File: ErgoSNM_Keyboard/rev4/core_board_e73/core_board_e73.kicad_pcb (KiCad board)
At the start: 2 copper layers, 50.8 x 36.2 mm, 55 parts, among them J1 USB_C_Receptacle_USB2.0, J2 USB_C_Receptacle_USB2.0, J3 Conn_01x30, J4 Conn_Batt, J5 Debug, SW1 SW_DPDT_x2, U1 E73-2G4M08S1C, U2 SRV05-4, U3 TPS63020, U4 BQ24075RGT, U5 SRV05-4, Y1 32.768kHz

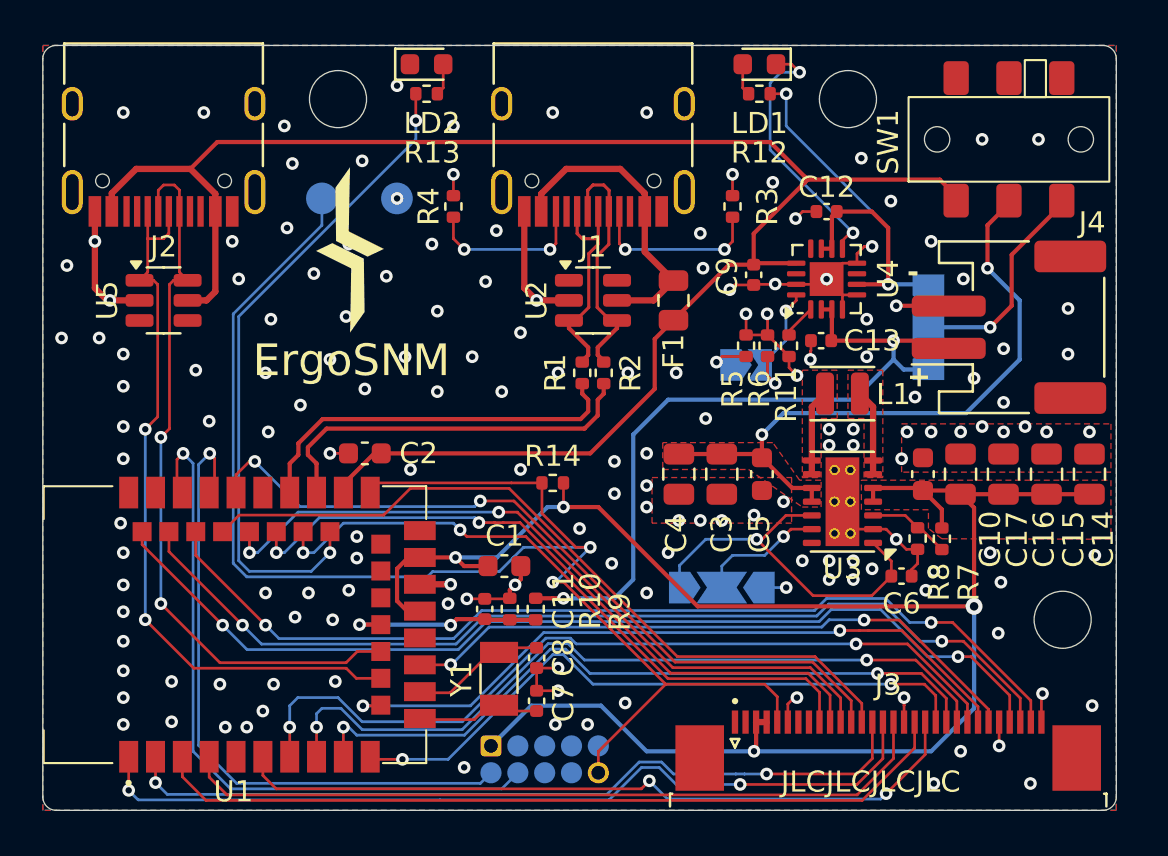
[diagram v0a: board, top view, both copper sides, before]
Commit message: feat: update USB ESD
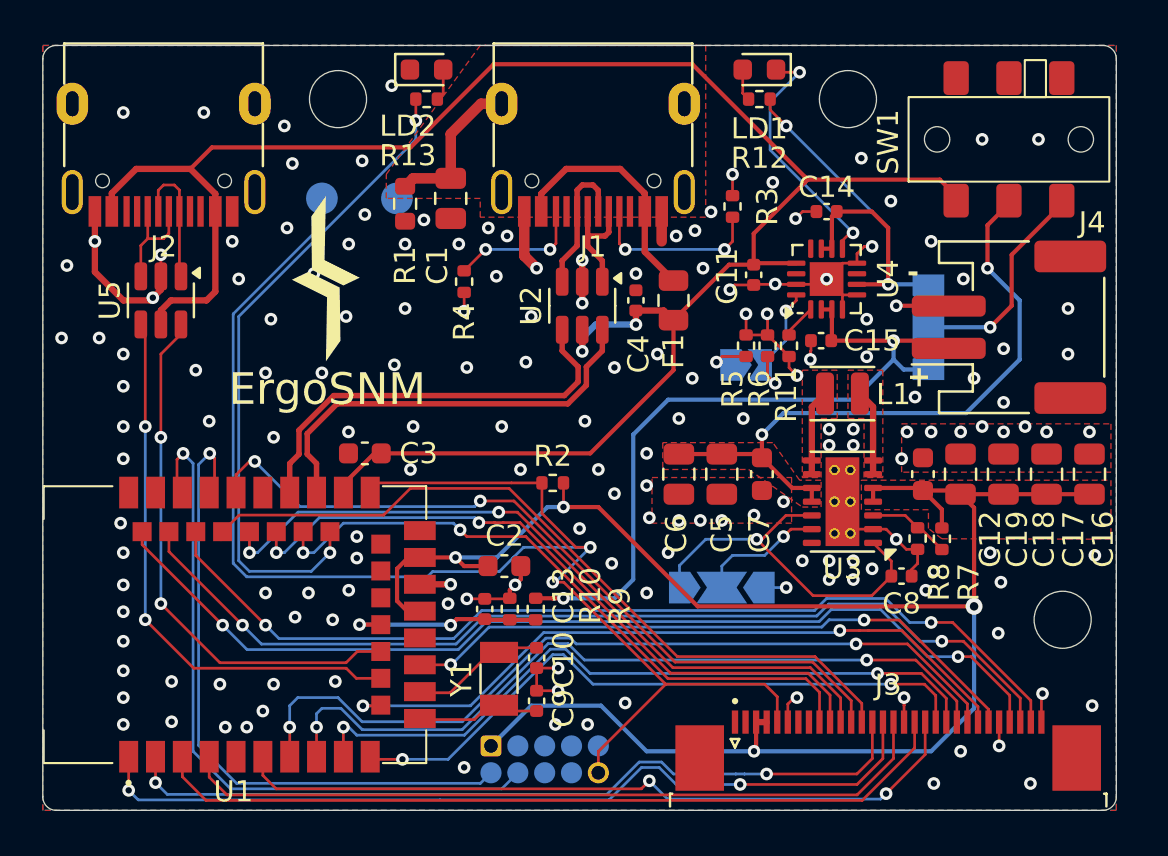
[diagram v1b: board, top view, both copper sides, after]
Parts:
- removed the R2 at (142.7, 100.6)
- added C1: 4.7nF, Capacitor_SMD:C_0805_2012Metric, F.Cu at (135.5, 92.3)
- added C4: 100nF, Capacitor_SMD:C_0402_1005Metric, F.Cu at (144.3, 97.2)
- R1: value 27R -> 1M; footprint Resistor_SMD:R_0402_1005Metric -> Resistor_SMD:R_0603_1608Metric
- R3, R4: value 5.1k -> 5.1k 1%
- U2, U5: value SRV05-4 -> USBLC6-2SC6
- moved R1 11.6 mm to (133.3, 92.6), turned to -90 degrees
- moved R4 3.59 mm to (136.1, 96.3), turned to -90 degrees
- moved U2 0.57 mm to (141.7, 97.4), turned to -90 degrees
- moved LD1 0.25 mm to (150.1, 86.2)
- moved LD2 0.25 mm to (134.4, 86.2)
- moved R12 0.25 mm to (150.1, 87.6)
- moved R13 0.25 mm to (134.4, 87.6)
- moved U5 0.13 mm to (121.8, 97.2), turned to -90 degrees
- renumbered C8 to C10, C9 to C11, C10 to C12, C11 to C13, C12 to C14, C13 to C15, C14 to C16, C15 to C17, C16 to C18, C17 to C19, C1 to C2, C2 to C3, C3 to C5, C4 to C6, C5 to C7, C6 to C8, C7 to C9, R14 to R2
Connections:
- J1 pad A6: USB_D+ -> /CONN_D+
- J1 pad A7: USB_D- -> /CONN_D-
- J1 pad B6: USB_D+ -> /CONN_D+
- J1 pad B7: USB_D- -> /CONN_D-
- J1 pad S1: GND -> /USB_SH
- J2 pad A6: TX -> Net-(J2-D+-PadA6)
- J2 pad A7: RX -> Net-(J2-D--PadA7)
- J2 pad B6: TX -> Net-(J2-D+-PadA6)
- J2 pad B7: RX -> Net-(J2-D--PadA7)
- R1 pad 1: /D+ -> /USB_SH
- R1 pad 2: USB_D+ -> GND
- U1 pad 29: /D- -> USB_D-
- U1 pad 31: /D+ -> USB_D+
- U2 pad 1: unconnected-(U2-IO1-Pad1) -> /CONN_D-
- U2 pad 3: USB_D+ -> /CONN_D+
- U2 pad 4: USB_D- -> USB_D+
- U2 pad 5: +5V -> VBUS
- U2 pad 6: unconnected-(U2-IO4-Pad6) -> USB_D-
- U5 pad 1: TX -> Net-(J2-D--PadA7)
- U5 pad 3: unconnected-(U5-IO2-Pad3) -> Net-(J2-D+-PadA6)
- U5 pad 4: unconnected-(U5-IO3-Pad4) -> TX
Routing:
- net /D-: track 18.8 -> 0.00 mm
- net /D+: track 18.8 -> 0.00 mm
- net VBUS: track 83.8 -> 96.0 mm, vias 0 -> 2
- net USB_D+: track 10.5 -> 20.6 mm
- net RX: track 34.6 -> 25.4 mm
- net USB_D-: track 11.7 -> 20.6 mm
- net TX: track 34.9 -> 26.4 mm
- net /USB_SH: track 0.00 -> 7.38 mm
- net /CONN_D+: track 0.00 -> 6.83 mm
- net Net-(J2-D--PadA7): track 0.00 -> 6.32 mm
- net /CONN_D-: track 0.00 -> 5.67 mm
- net Net-(J2-D+-PadA6): track 0.00 -> 5.35 mm
- net +5V: track 14.5 -> 11.4 mm
- net GND: track 54.1 -> 56.0 mm, vias 162 -> 168
- net Net-(J1-CC2): track 7.71 -> 6.40 mm
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- added copper zone on F.Cu, net /USB_SH
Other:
- board text added: "Unit: mm"

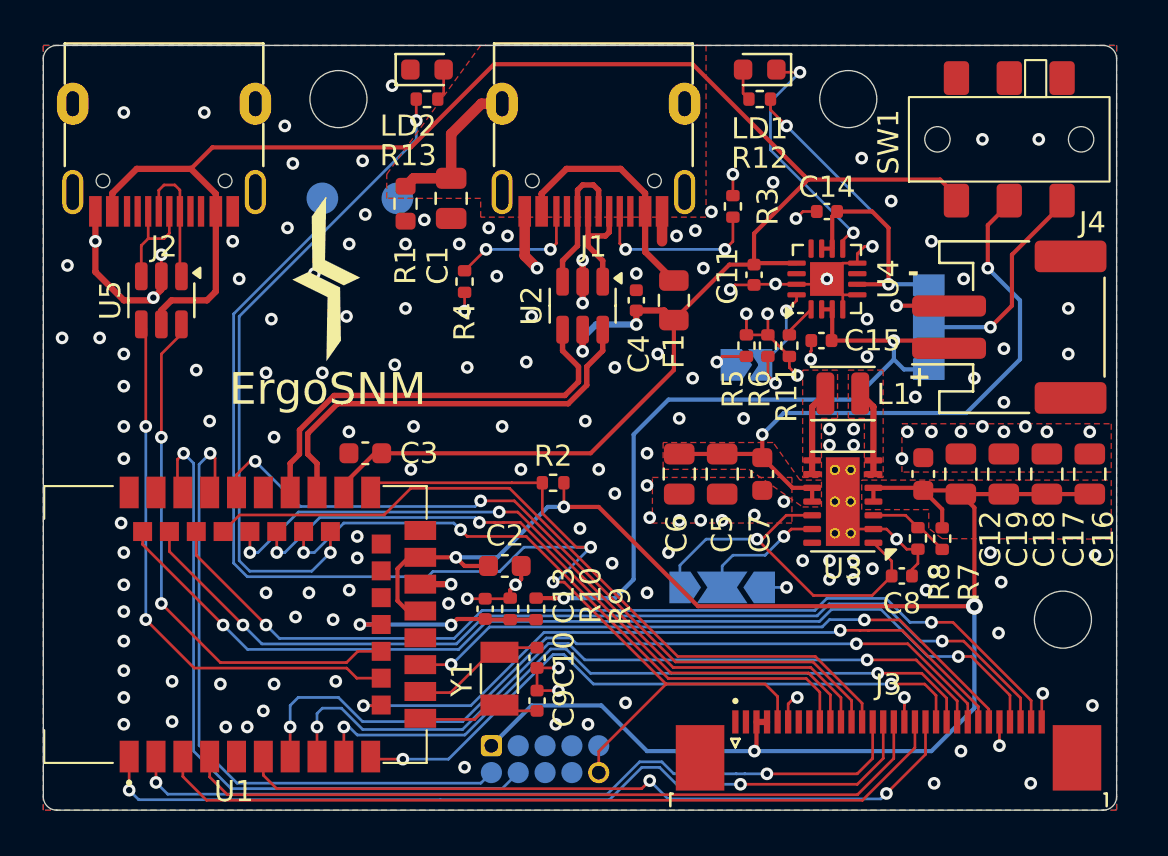
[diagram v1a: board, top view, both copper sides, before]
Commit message: feat: change Buck-Boost DC/DC IC from TPS63020 to TPS63900
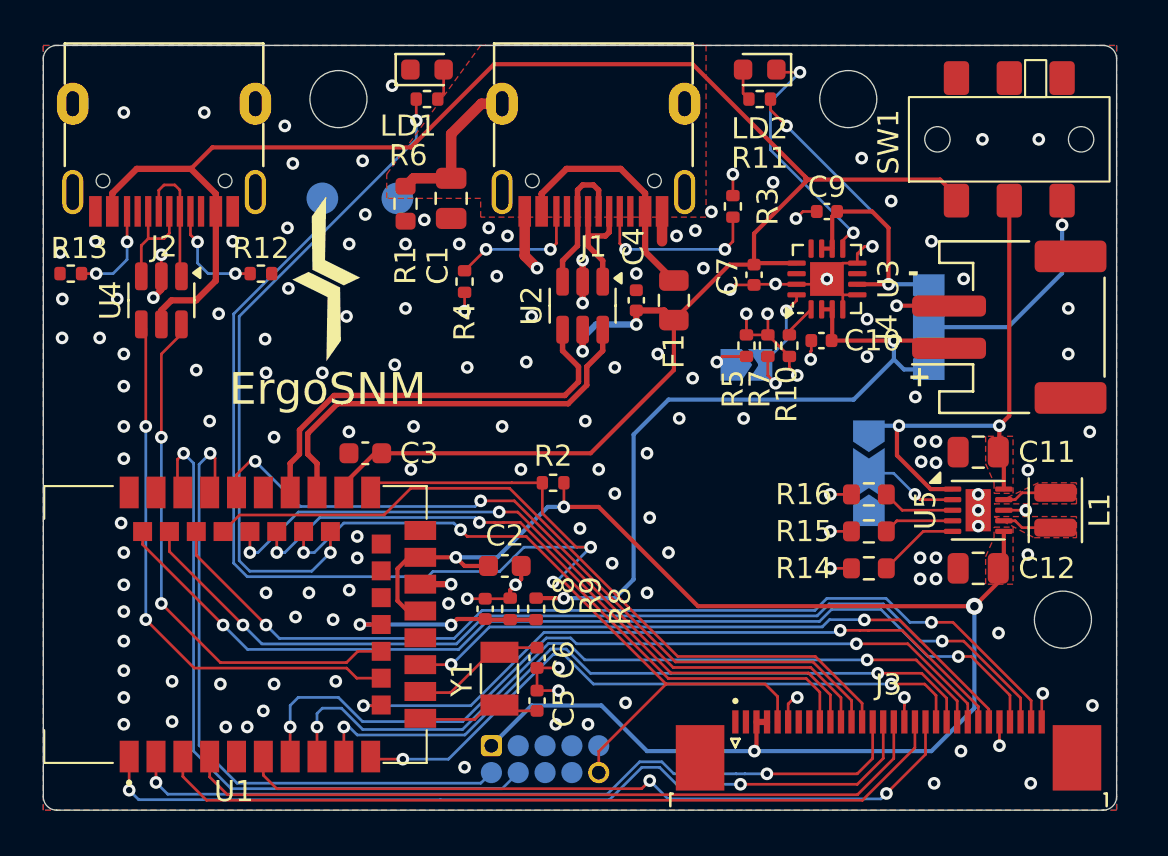
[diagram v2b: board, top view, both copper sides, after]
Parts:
- removed C16, C17, C18, C19: 22uF, Capacitor_SMD:C_0805_2012Metric
- removed the C5 at (148.3, 105.4)
- removed the C6 at (146.3, 105.4)
- removed the C7 at (150.2, 105.4)
- removed the C8 at (156.8, 110.2)
- removed the R7 at (158.8, 108.4)
- removed the R8 at (157.6, 108.4)
- removed the U3 at (154.0, 106.7)
- added C11: 22uF, Capacitor_SMD:C_0805_2012Metric, F.Cu at (160.5, 104.3)
- added R12: 5.1k 1%, Resistor_SMD:R_0402_1005Metric, F.Cu at (126.5, 95.9)
- added R13: 5.1k 1%, Resistor_SMD:R_0402_1005Metric, F.Cu at (117.5, 95.9)
- added R14: 1.2k 1%, Resistor_SMD:R_0603_1608Metric, F.Cu at (155.3, 109.8)
- added R15: 0R 1%, Resistor_SMD:R_0603_1608Metric, F.Cu at (155.3, 108.1)
- added R16: 30k 1%, Resistor_SMD:R_0603_1608Metric, F.Cu at (155.3, 106.3)
- added U5: TPS63900, Package_SON:WSON-10-1EP_2.5x2.5mm_P0.5mm_EP1.2x2mm, F.Cu at (160.5, 107.1)
- C12: value 2.2uF -> 22uF; footprint Capacitor_SMD:C_0603_1608Metric -> Capacitor_SMD:C_0805_2012Metric
- L1: value 1.5uH -> 2.2uH
- SB3: renamed from SB2; value Power Save -> VDD Selection
- moved L1 11.5 mm to (164.1, 107.1), turned to 90 degrees
- moved SB3 8.80 mm to (155.3, 105.3), turned to -90 degrees
- moved C12 5.17 mm to (160.5, 109.8), turned to 180 degrees
- turned C4 to 90 degrees
- renumbered C15 to C10, C9 to C5, C10 to C6, C11 to C7, C13 to C8, C14 to C9, LD2 to LD1, LD1 to LD2, R11 to R10, R12 to R11, R13 to R6, R6 to R7, R9 to R8, R10 to R9, SB3 to SB1, SB1 to SB2, U4 to U3, U5 to U4
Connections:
- C4 pad 1: GND -> VBUS
- C4 pad 2: VBUS -> GND
- J2 pad A5: unconnected-(J2-CC1-PadA5) -> Net-(J2-CC1)
- J2 pad B5: unconnected-(J2-CC2-PadB5) -> Net-(J2-CC2)
- J3 pad MP: (no net) -> unconnected-(J3-MountPin-PadMP)_1
- J4 pad MP: (no net) -> unconnected-(J4-MountPin-PadMP)
- SB3 pad 1: /VINA -> /VIN_DCDC
- SB3 pad 2: /PWR_SAVE -> /VDD_SEL
- SW1 pad 2: Net-(SW1A-B) -> /VIN_DCDC
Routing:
- net Net-(SW1A-B): track 30.9 -> 0.00 mm, vias 2 -> 0
- net /VIN_DCDC: track 0.00 -> 25.0 mm, vias 0 -> 2
- net /VINA: track 18.1 -> 0.00 mm, vias 1 -> 0
- net VDD: track 87.6 -> 73.0 mm
- net GND: track 56.0 -> 47.7 mm, vias 168 -> 153
- net /PWR_SAVE: track 6.00 -> 0.00 mm, vias 1 -> 0
- net Net-(J2-CC1): track 0.00 -> 5.28 mm, vias 0 -> 2
- net Net-(J2-CC2): track 0.00 -> 4.71 mm, vias 0 -> 2
- net /VDD_SEL: track 0.00 -> 4.48 mm, vias 0 -> 1
- net Net-(U3-FB): track 3.92 -> 0.00 mm
- net Net-(U5-CFG3): track 0.00 -> 3.86 mm
- net Net-(U5-CFG1): track 0.00 -> 3.45 mm
- net Net-(U5-CFG2): track 0.00 -> 3.34 mm
- net Net-(U5-LX2): track 4.07 -> 2.57 mm
- net Net-(U5-LX1): track 4.07 -> 2.57 mm
- added copper zone on F.Cu, net /VIN_DCDC
- removed copper zone on F.Cu, net Net-(SW1A-B)

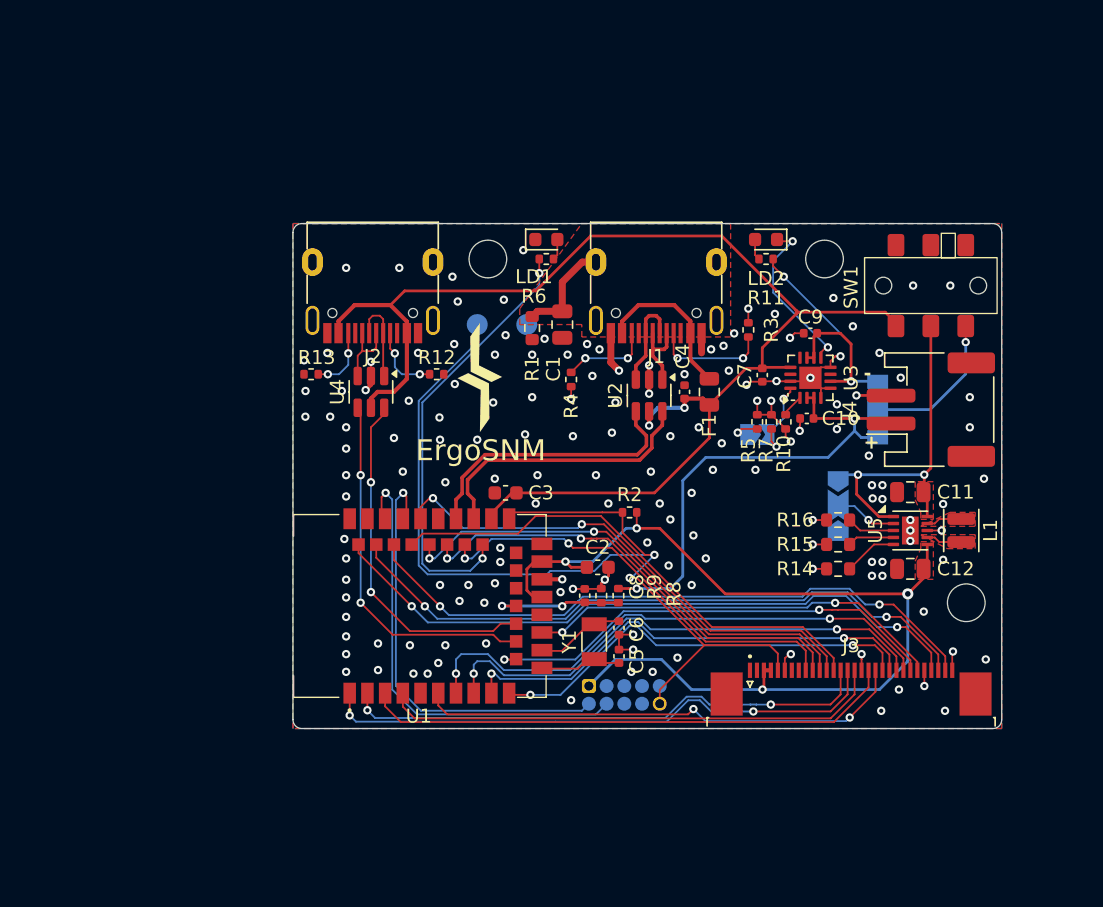
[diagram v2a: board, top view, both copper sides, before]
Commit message: feat: change pin header position
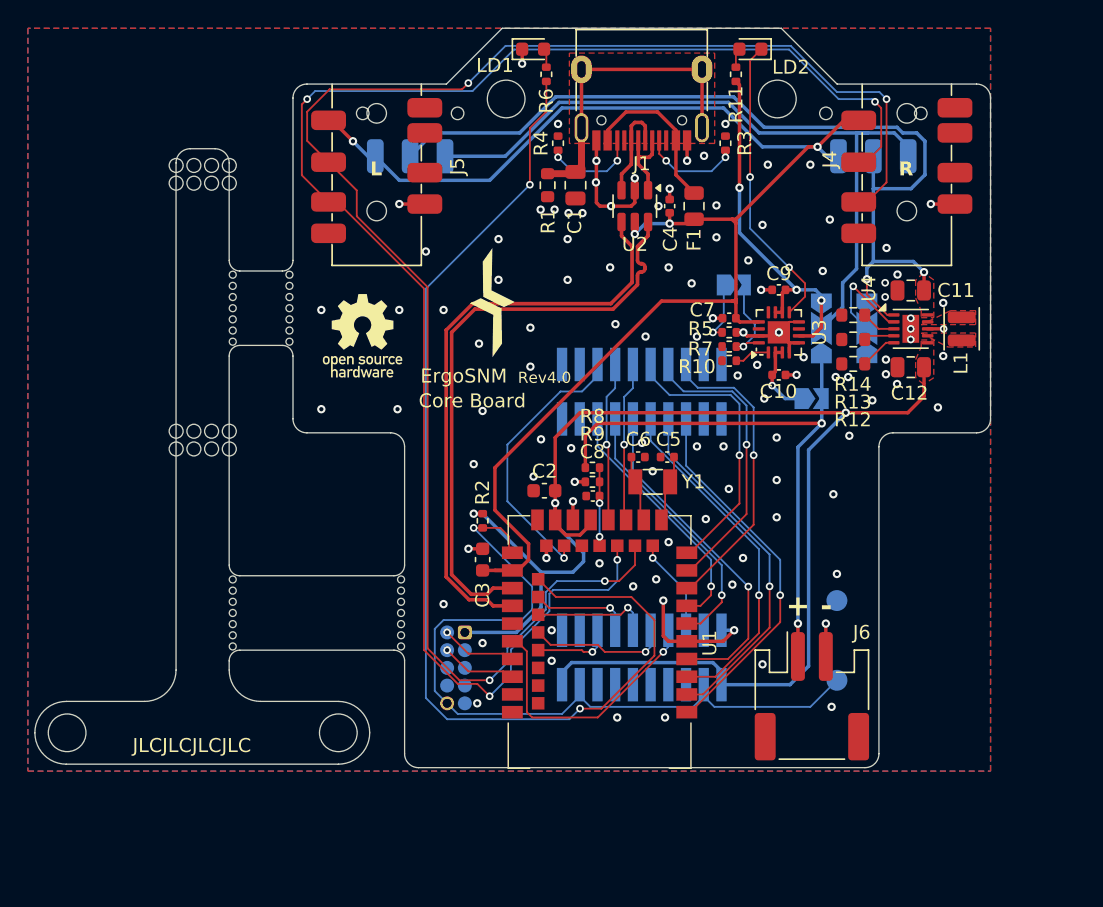
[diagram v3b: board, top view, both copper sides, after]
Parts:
- removed the R12 at (126.5, 95.9)
- removed the R13 at (117.5, 95.9)
- removed the U4 at (121.8, 97.2)
- added H23: MountingHole, ErgoSNM_Keyboard:mouse_bit, F.Cu at (111.9, 113.0)
- added H4: MountingHole, MountingHole:MountingHole_2.7mm_M2.5_ISO7380, F.Cu at (100.0, 121.6)
- added H5: MountingHole, ErgoSNM_Keyboard:mouse_bit, F.Cu at (111.9, 91.2)
- added H6: MountingHole, ErgoSNM_Keyboard:mouse_bit, F.Cu at (116.0, 91.2)
- added H7: MountingHole, ErgoSNM_Keyboard:mouse_bit, F.Cu at (124.0, 113.0)
- added J4: PJ-393_TRRS_8P, ErgoSNM_Keyboard:PJ-393 8P TRRS, F.Cu at (160.2, 80.5)
- added J5: PJ-393_TRRS_8P, ErgoSNM_Keyboard:PJ-393 8P TRRS, F.Cu at (122.2, 80.5)
- added J8: Conn_02x05_Odd_Even, Connector_PinHeader_1.27mm:PinHeader_2x04_P1.27mm_Vertical, F.Cu at (111.6, 100.0)
- added J9: Conn_02x05_Odd_Even, Connector_PinHeader_1.27mm:PinHeader_2x04_P1.27mm_Vertical, F.Cu at (111.6, 80.9)
- added SB2: LiPo_CHG, Jumper:SolderJumper-2_P1.3mm_Open_TrianglePad1.0x1.5mm, B.Cu at (153.4, 97.6)
- added SW2: SW_SPDT, ErgoSNM_Keyboard:9_3.5_3.5_switch, B.Cu at (124.6, 77.2)
- J2: value USB_C_Receptacle_USB2.0 -> Conn_02x10_Odd_Even; footprint Connector_USB:USB_C_Receptacle_HRO_TYPE-C-31-M-12 -> Connector_PinHeader_1.27mm:PinHeader_2x10_P1.27mm_Vertical_SMD; moved to B.Cu
- J3: value Conn_01x30 -> Conn_02x10_Odd_Even; footprint Connector_FFC-FPC:TE_3-1734839-0_1x30-1MP_P0.5mm_Horizontal -> Connector_PinHeader_1.27mm:PinHeader_2x10_P1.27mm_Vertical_SMD; moved to B.Cu
- SW1: value SW_DPDT_x2 -> SW_SPDT; footprint ErgoSNM_Keyboard:MSKT-22D14-T -> ErgoSNM_Keyboard:9_3.5_3.5_switch; moved to B.Cu
- moved H3 46.0 mm to (119.5, 121.6)
- moved TP1 36.3 mm to (155.2, 117.8)
- moved TP2 29.8 mm to (155.2, 112.1)
- moved H2 25.5 mm to (131.5, 76.2)
- moved H1 23.7 mm to (150.9, 76.2)
- moved J6 22.2 mm to (153.4, 119.0), turned to 0 degrees
- moved J2 21.0 mm to (141.2, 97.1), turned to 90 degrees
- moved R4 17.0 mm to (135.2, 79.3), turned to 90 degrees
- moved J3 15.2 mm to (141.2, 116.2), turned to 90 degrees
- moved R12 14.7 mm to (156.4, 95.1)
- moved R13 14.7 mm to (156.4, 93.4)
- moved R14 14.7 mm to (156.4, 91.6)
- moved C5 14.7 mm to (143.0, 101.8), turned to 0 degrees
- moved C11 14.5 mm to (160.5, 89.9)
- moved C12 14.5 mm to (160.5, 95.4)
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- renumbered J4 to J6, J5 to J7, R14 to R12, R15 to R13, R16 to R14, SB2 to SB3, SB3 to SB4, U5 to U4
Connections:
- net /VDD_SEL renamed /OUT_SEL
- net Net-(SB2-C) renamed /VBATT_SRC
- C10 pad 2: +BATT -> Net-(SB2-A)
- J3 pad 1: unconnected-(J3-Pin_1-Pad1) -> VDD
- J3 pad 10: SCLK -> HS_IO_2
- J3 pad 11: MOSI -> unconnected-(J3-Pin_11-Pad11)
- J3 pad 12: MISO -> HS_IO_3
- J3 pad 13: nCS -> unconnected-(J3-Pin_13-Pad13)
- J3 pad 14: ROW_0 -> HS_IO_4
- J3 pad 15: ROW_1 -> unconnected-(J3-Pin_15-Pad15)
- J3 pad 16: ROW_2 -> HS_IO_5
- J3 pad 17: GND -> RESET
- J3 pad 18: ROW_3 -> unconnected-(J3-Pin_18-Pad18)
- J3 pad 19: ROW_4 -> VDD
- J3 pad 2: unconnected-(J3-Pin_2-Pad2) -> GND
- J3 pad 20: COL_0 -> GND
- J3 pad 3: VDD -> RESET
- J3 pad 4: VDD -> unconnected-(J3-Pin_4-Pad4)
- J3 pad 5: RESET -> unconnected-(J3-Pin_5-Pad5)
- J3 pad 6: GND -> HS_IO_0
- J3 pad 8: unconnected-(J3-Pin_8-Pad8) -> HS_IO_1
- J3 pad 9: MOTION -> unconnected-(J3-Pin_9-Pad9)
- SB4 pad 1: /VIN_DCDC -> GND
- SB4 pad 3: GND -> /VIN_DCDC
- U1 pad 1: ROW_1 -> ROW_IO_0
- U1 pad 10: COL_0 -> COL_IO_2
- U1 pad 12: COL_4 -> HS_IO_0
- U1 pad 15: COL_5 -> COL_IO_3
- U1 pad 17: unconnected-(U1-P1.09-Pad17) -> COL_IO_4
- U1 pad 2: ROW_0 -> ROW_IO_1
- U1 pad 22: unconnected-(U1-P0.07-Pad22) -> COL_IO_5
- U1 pad 3: ROW_3 -> ROW_IO_2
- U1 pad 30: MOTION -> HS_IO_4
- U1 pad 32: SCLK -> HS_IO_3
- U1 pad 34: MOSI -> HS_IO_2
- U1 pad 35: MISO -> HS_IO_1
- U1 pad 36: nCS -> HS_IO_5
- U1 pad 38: IO_2 -> unconnected-(U1-P1.02-Pad38)
- U1 pad 4: ROW_2 -> ROW_IO_3
- U1 pad 40: IO_1 -> unconnected-(U1-P1.04-Pad40)
- U1 pad 42: IO_0 -> unconnected-(U1-P1.06-Pad42)
- U1 pad 6: ROW_4 -> ROW_IO_4
- U1 pad 7: COL_3 -> ROW_IO_5
- U1 pad 8: COL_2 -> COL_IO_0
- U1 pad 9: COL_1 -> COL_IO_1
- U3 pad 2: +BATT -> Net-(SB2-A)
- U3 pad 3: +BATT -> Net-(SB2-A)
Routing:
- net TX: track 26.4 -> 117.6 mm, vias 2 -> 4
- net RX: track 25.4 -> 115.8 mm, vias 2 -> 4
- net STATUS_LED: track 31.2 -> 78.8 mm
- net IO_0: track 47.1 -> 0.00 mm, vias 2 -> 0
- net IO_1: track 46.8 -> 0.00 mm, vias 2 -> 0
- net IO_2: track 46.1 -> 0.00 mm, vias 2 -> 0
- net /VBATT_SRC: track 10.8 -> 52.7 mm, vias 1 -> 0
- net /VIN_DCDC: track 25.0 -> 65.9 mm
- net ROW_1: track 40.4 -> 0.00 mm, vias 2 -> 0
- net COL_3: track 39.2 -> 0.00 mm, vias 2 -> 0
- net ROW_3: track 38.1 -> 0.00 mm
- net ROW_0: track 38.0 -> 0.00 mm, vias 2 -> 0
- net COL_2: track 36.9 -> 0.00 mm, vias 2 -> 0
- net nCS: track 36.4 -> 0.00 mm
- net MISO: track 35.9 -> 0.00 mm, vias 2 -> 0
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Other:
- board size 50.8 x 36.2 mm -> 68.5 x 53 mm
- board text added: "Core Board"
- board text added: "L"
- board text added: "R"
- board text added: "Rev${REVISION}"
